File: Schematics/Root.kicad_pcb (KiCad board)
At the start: 2 copper layers, 100 x 100 mm, 137 parts, among them CON1 USB-MICRO-B, CON2 BARREL_JACK, IC1 ATXMEGA256A3BU-A, J1 AVR_JTAG_Header, P1 CONN_02X08, SW1 SW_PUSH, SW2 SW_PUSH, SW3 SW_PUSH, SW4 SW_PUSH, U1 PCA9685, U10 PCA9685, U11 PCA9685, U12 PCA9685, U13 LT8612, U2 PCA9685, U3 PCA9685, U4 PCA9685, U5 PCA9685, U6 PCA9685, U7 PCA9685, U8 PCA9685, U9 PCA9685, X1 16MHz, X2 32.768KhZ

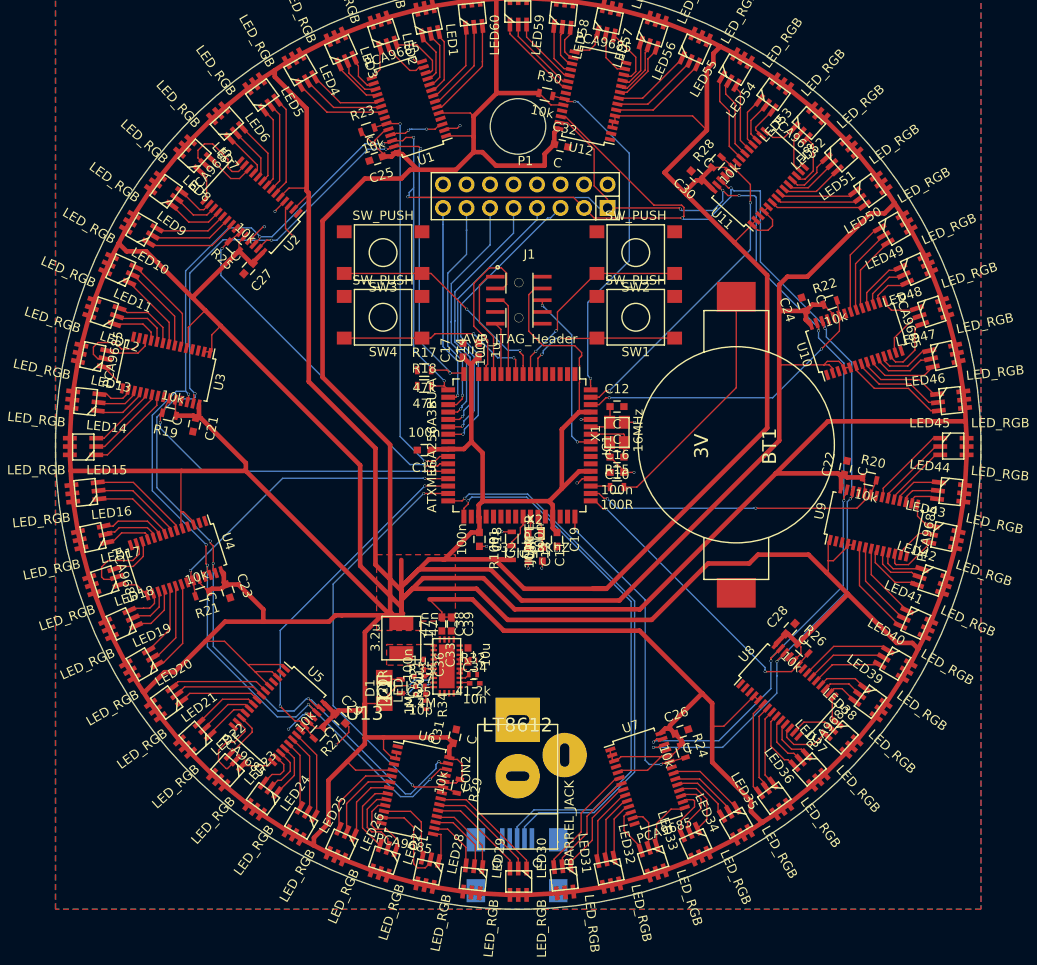
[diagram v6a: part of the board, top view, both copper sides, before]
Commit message: Main GND plane added.
Need to add island plane for SMPS
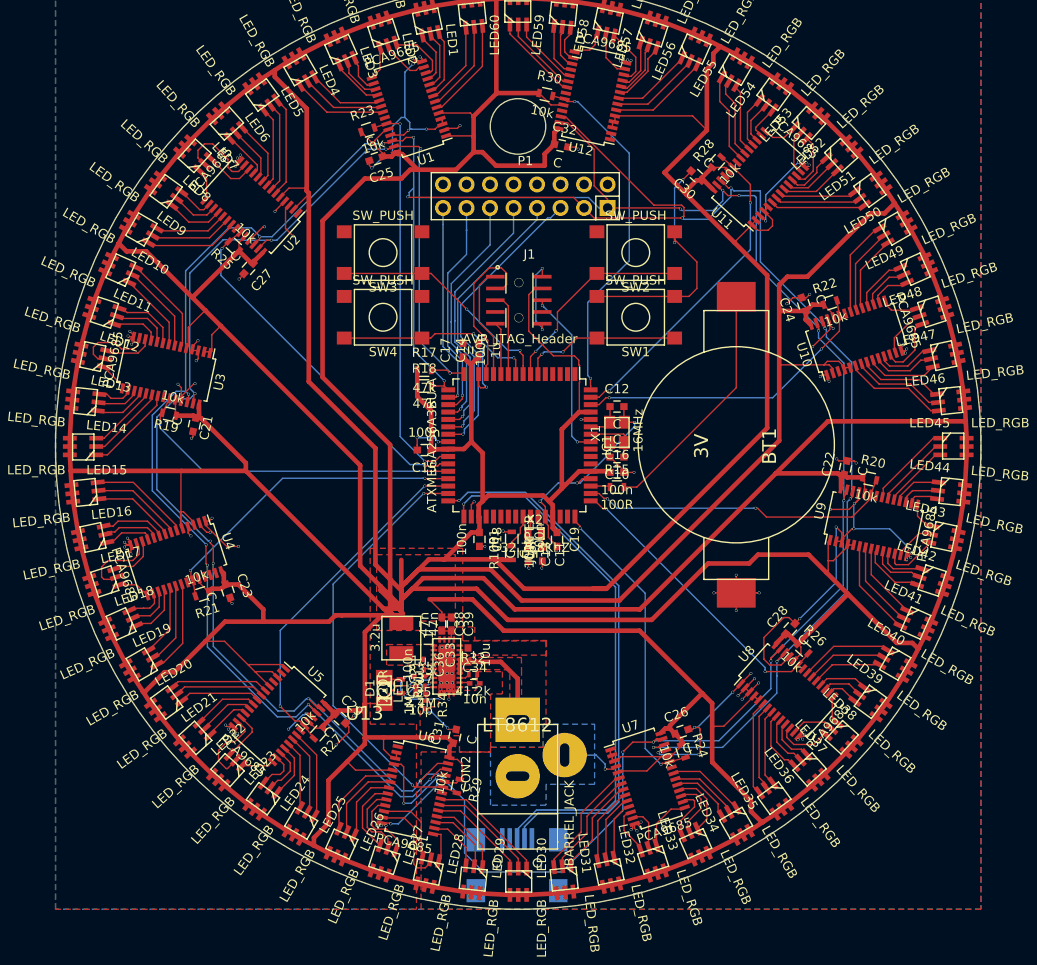
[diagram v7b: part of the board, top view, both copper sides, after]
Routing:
- net GND: track 36.2 -> 360.7 mm, vias 19 -> 141
- net /Display/SDA: track 279.0 -> 322.0 mm, vias 16 -> 17
- net VPP: track 1347.9 -> 1368.5 mm
- net /Power Supply/Vin: track 0.00 -> 12.9 mm
- net /Display/Display Sub block 9/~OE: track 33.2 -> 34.2 mm
- net /Display/Display Sub block 7/~OE: track 34.7 -> 34.0 mm
- net /Microcontroller/USB_D+: track 58.9 -> 58.2 mm
